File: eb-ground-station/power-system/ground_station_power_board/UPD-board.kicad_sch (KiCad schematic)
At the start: 101 parts, among them J1 Conn_01x04, J10 PI 1827486, J11 PC 1720806, J12 Conn_02x02_Odd_Even, J13 Conn_01x05, J14 Conn_01x04, J2 Conn_01x03, J3 Conn_01x03, J4 Conn_01x03, J5 Conn_01x03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

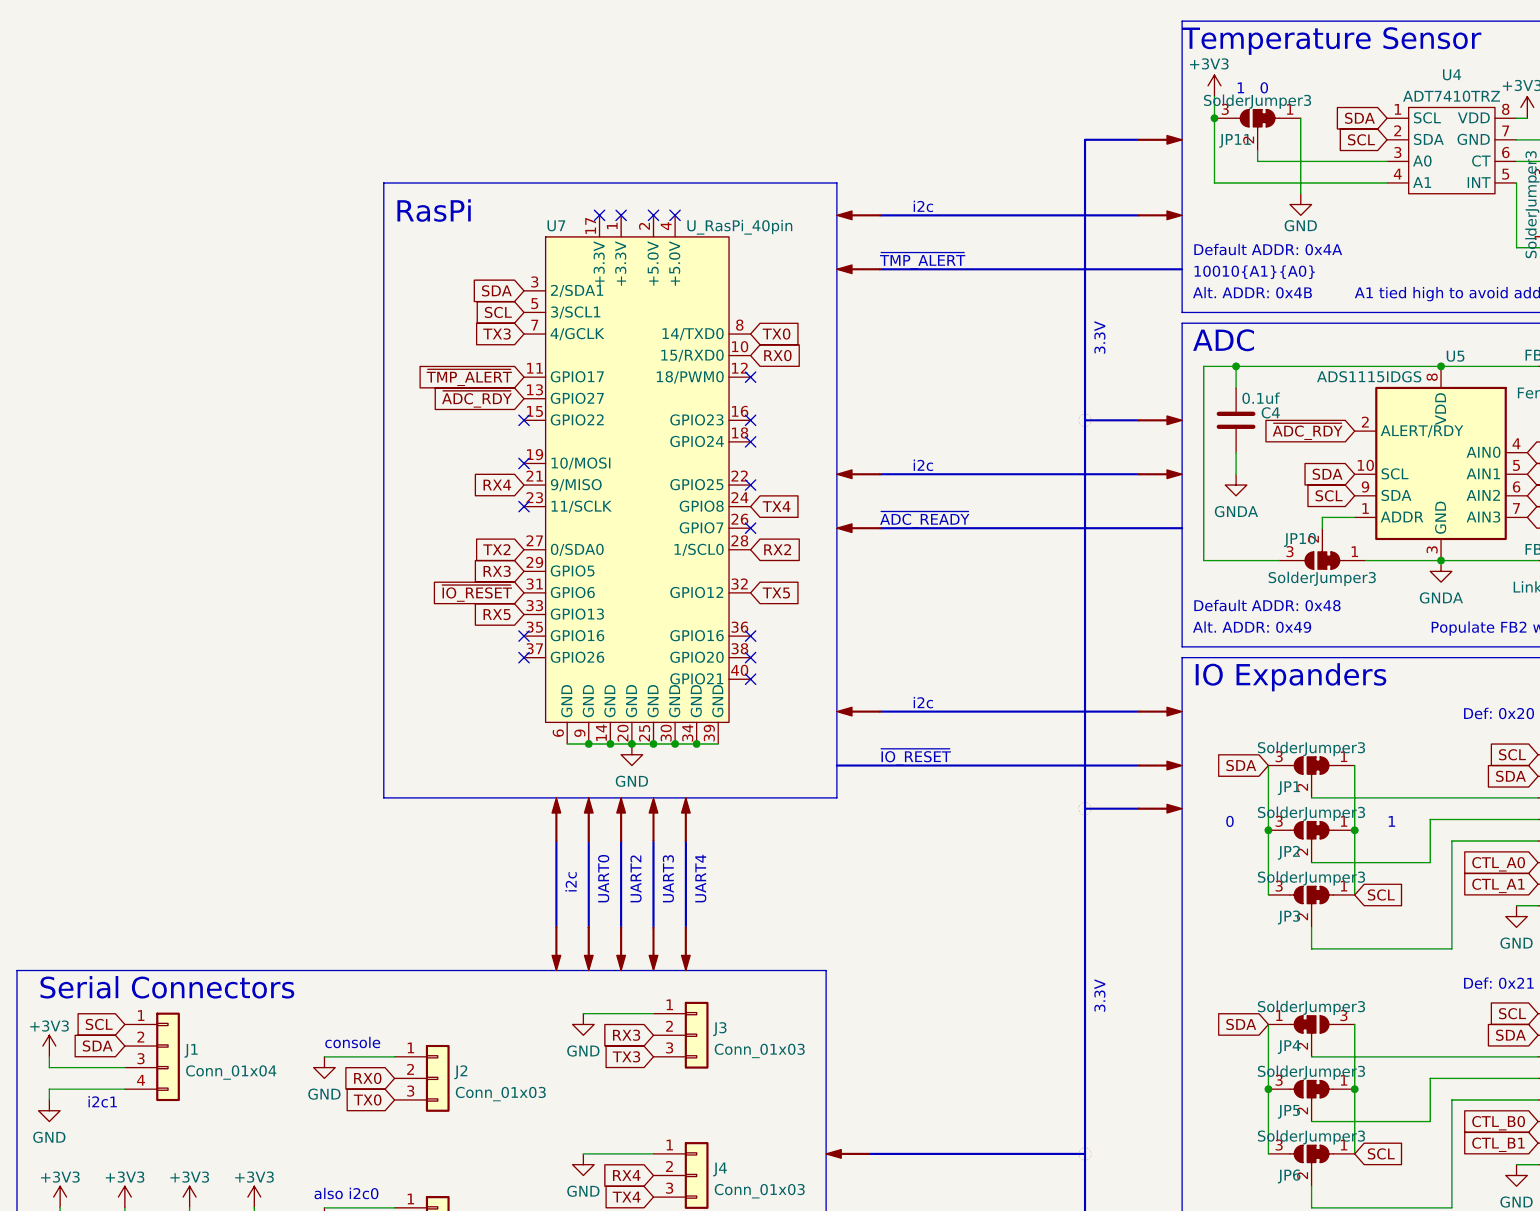
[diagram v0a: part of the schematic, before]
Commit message: Fixed UPD board, ready for review and ordering
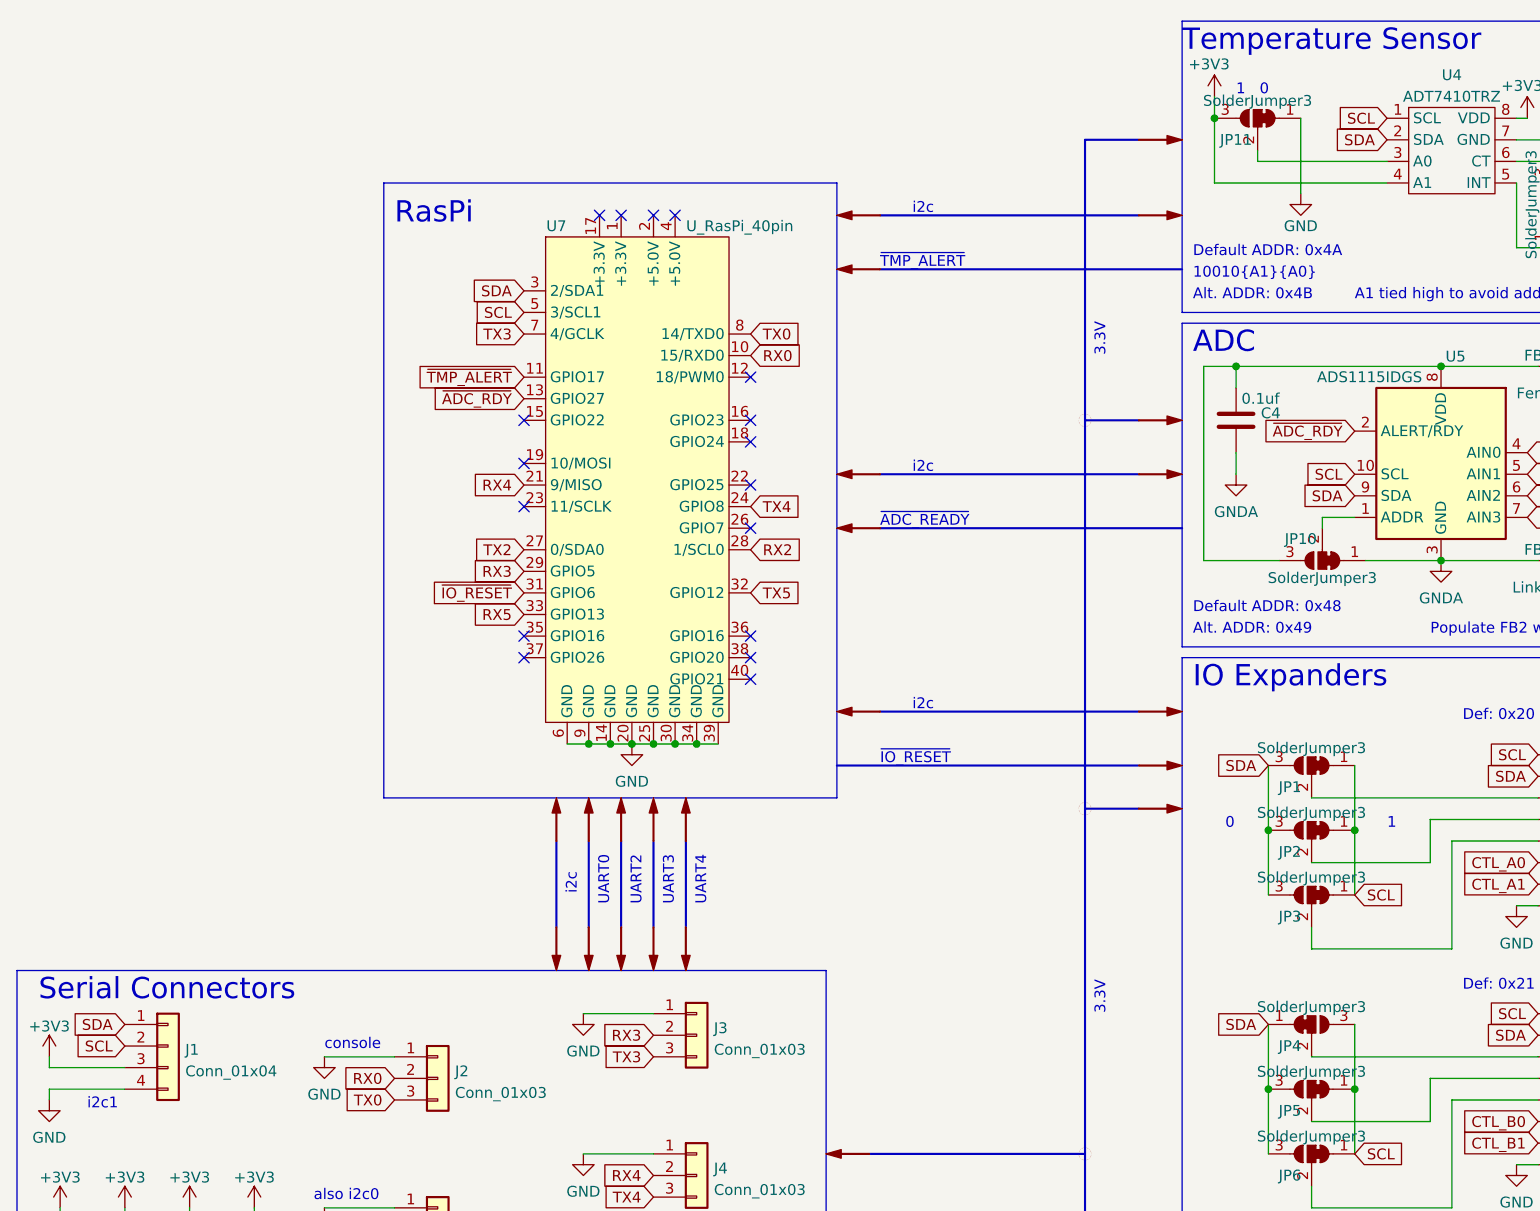
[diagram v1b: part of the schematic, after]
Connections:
- net SCL: now also J1.2 (Pin_2), U4.1 (SCL), U5.10 (SCL); no longer J1.1 (Pin_1), U4.2 (SDA), U5.9 (SDA)
- net SDA: now also J1.1 (Pin_1), U4.2 (SDA), U5.9 (SDA); no longer J1.2 (Pin_2), U4.1 (SCL), U5.10 (SCL)
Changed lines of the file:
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@@
     )
   )
-  (global_label "SDA" (shape input) (at 184.15 68.58 180) (fields_autoplaced)
+  (global_label "SDA" (shape input) (at 184.15 71.12 180) (fields_autoplaced)
     (effects (font (size 1.27 1.27)) (justify right))
-    (property "Intersheet References" "${INTERSHEET_REFS}" (id 0) (at 178.1688 68.5006 0)
+    (property "Intersheet References" "${INTERSHEET_REFS}" (id 0) (at 178.1688 71.0406 0)
       (effects (font (size 1.27 1.27)) (justify right) hide)
     )
@@
     )
   )
-  (global_label "SDA" (shape input) (at 187.96 26.67 180) (fields_autoplaced)
+  (global_label "SDA" (shape input) (at 187.96 29.21 180) (fields_autoplaced)
     (effects (font (size 1.27 1.27)) (justify right))
-    (property "Intersheet References" "${INTERSHEET_REFS}" (id 0) (at 181.9788 26.5906 0)
+    (property "Intersheet References" "${INTERSHEET_REFS}" (id 0) (at 181.9788 29.1306 0)
       (effects (font (size 1.27 1.27)) (justify right) hide)
     )
@@
     )
   )
-  (global_label "SDA" (shape input) (at 39.37 135.89 180) (fields_autoplaced)
+  (global_label "SDA" (shape input) (at 39.37 133.35 180) (fields_autoplaced)
     (effects (font (size 1.27 1.27)) (justify right))
-    (property "Intersheet References" "${INTERSHEET_REFS}" (id 0) (at 33.3888 135.8106 0)
+    (property "Intersheet References" "${INTERSHEET_REFS}" (id 0) (at 33.3888 133.2706 0)
       (effects (font (size 1.27 1.27)) (justify right) hide)
     )
@@
     )
   )
-  (global_label "SCL" (shape input) (at 39.37 133.35 180) (fields_autoplaced)
+  (global_label "SCL" (shape input) (at 39.37 135.89 180) (fields_autoplaced)
     (effects (font (size 1.27 1.27)) (justify right))
-    (property "Intersheet References" "${INTERSHEET_REFS}" (id 0) (at 33.4493 133.2706 0)
+    (property "Intersheet References" "${INTERSHEET_REFS}" (id 0) (at 33.4493 135.8106 0)
       (effects (font (size 1.27 1.27)) (justify right) hide)
     )
@@
     )
   )
-  (global_label "SCL" (shape input) (at 187.96 29.21 180) (fields_autoplaced)
+  (global_label "SCL" (shape input) (at 187.96 26.67 180) (fields_autoplaced)
     (effects (font (size 1.27 1.27)) (justify right))
-    (property "Intersheet References" "${INTERSHEET_REFS}" (id 0) (at 182.0393 29.1306 0)
+    (property "Intersheet References" "${INTERSHEET_REFS}" (id 0) (at 182.0393 26.5906 0)
       (effects (font (size 1.27 1.27)) (justify right) hide)
     )
@@
     )
   )
-  (global_label "SCL" (shape input) (at 184.15 71.12 180) (fields_autoplaced)
+  (global_label "SCL" (shape input) (at 184.15 68.58 180) (fields_autoplaced)
     (effects (font (size 1.27 1.27)) (justify right))
-    (property "Intersheet References" "${INTERSHEET_REFS}" (id 0) (at 178.2293 71.0406 0)
+    (property "Intersheet References" "${INTERSHEET_REFS}" (id 0) (at 178.2293 68.5006 0)
       (effects (font (size 1.27 1.27)) (justify right) hide)
     )
@@
       (reference "LOGO1") (unit 1) (value "OreSat Logo") (footprint "oresat-footprints:logo-small")
     )
-    (path "/3a1c5476-bb6a-4918-80d3-82e1846e9dbb/6f338c88-571d-40d4-a656-bab0f745db42"
+    (path "/3a1c5476-bb6a-4918-80d3-82e1846e9dbb/9b268302-c8f9-4880-a801-2f518477b68a"
       (reference "Q1") (unit 1) (value "DMN61D8L-LVT") (footprint "oresat-footprints:TSOT26-6")
     )
-    (path "/3a1c5476-bb6a-4918-80d3-82e1846e9dbb/9b268302-c8f9-4880-a801-2f518477b68a"
+    (path "/3a1c5476-bb6a-4918-80d3-82e1846e9dbb/6f338c88-571d-40d4-a656-bab0f745db42"
       (reference "Q1") (unit 2) (value "DMN61D8L-LVT") (footprint "oresat-footprints:TSOT26-6")
     )
@@
       (reference "Q3") (unit 1) (value "SUD50P08-25L-E3") (footprint "oresat-footprints:TO-252-3_TabIsPin2")
     )
-    (path "/3a1c5476-bb6a-4918-80d3-82e1846e9dbb/94011d84-c031-4181-9a68-89df89d536a3"
+    (path "/3a1c5476-bb6a-4918-80d3-82e1846e9dbb/deaca104-2c5f-455a-9001-3371e3306116"
       (reference "Q4") (unit 1) (value "DMN61D8L-LVT") (footprint "oresat-footprints:TSOT26-6")
     )
-    (path "/3a1c5476-bb6a-4918-80d3-82e1846e9dbb/deaca104-2c5f-455a-9001-3371e3306116"
+    (path "/3a1c5476-bb6a-4918-80d3-82e1846e9dbb/94011d84-c031-4181-9a68-89df89d536a3"
       (reference "Q4") (unit 2) (value "DMN61D8L-LVT") (footprint "oresat-footprints:TSOT26-6")
     )
@@
       (reference "Q6") (unit 1) (value "SUD50P08-25L-E3") (footprint "oresat-footprints:TO-252-3_TabIsPin2")
     )
-    (path "/3a1c5476-bb6a-4918-80d3-82e1846e9dbb/11b9c0f2-a612-4d52-85f4-d7fb97bd55bd"
+    (path "/3a1c5476-bb6a-4918-80d3-82e1846e9dbb/12ff1775-db0b-4f93-8454-17de940e4617"
       (reference "Q7") (unit 1) (value "DMN61D8L-LVT") (footprint "oresat-footprints:TSOT26-6")
     )
-    (path "/3a1c5476-bb6a-4918-80d3-82e1846e9dbb/12ff1775-db0b-4f93-8454-17de940e4617"
+    (path "/3a1c5476-bb6a-4918-80d3-82e1846e9dbb/11b9c0f2-a612-4d52-85f4-d7fb97bd55bd"
       (reference "Q7") (unit 2) (value "DMN61D8L-LVT") (footprint "oresat-footprints:TSOT26-6")
     )
@@
       (reference "Q9") (unit 1) (value "SUD50P08-25L-E3") (footprint "oresat-footprints:TO-252-3_TabIsPin2")
     )
-    (path "/3a1c5476-bb6a-4918-80d3-82e1846e9dbb/777a7611-3f95-4b63-882e-22837a921249"
+    (path "/3a1c5476-bb6a-4918-80d3-82e1846e9dbb/7846e60b-2e16-4833-b5a0-71b3e5a6fdb8"
       (reference "Q10") (unit 1) (value "DMN61D8L-LVT") (footprint "oresat-footprints:TSOT26-6")
     )
-    (path "/3a1c5476-bb6a-4918-80d3-82e1846e9dbb/7846e60b-2e16-4833-b5a0-71b3e5a6fdb8"
+    (path "/3a1c5476-bb6a-4918-80d3-82e1846e9dbb/777a7611-3f95-4b63-882e-22837a921249"
       (reference "Q10") (unit 2) (value "DMN61D8L-LVT") (footprint "oresat-footprints:TSOT26-6")
     )

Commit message: Fixed pin 1 of expanders being pulldown only
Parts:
- LOGO1: footprint oresat-footprints:logo-small -> oresat-graphics:logo-small
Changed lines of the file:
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@@
     )
     (property "Value" "OreSat Logo" (id 1) (at 410.21 259.08 0))
-    (property "Footprint" "oresat-footprints:logo-small" (id 2) (at 402.59 259.08 0)
+    (property "Footprint" "oresat-graphics:logo-small" (id 2) (at 402.59 259.08 0)
       (effects (font (size 1.27 1.27)) hide)
     )
@@
       (reference "#PWR0109") (unit 1) (value "GND") (footprint "")
     )
+    (path "/3a1c5476-bb6a-4918-80d3-82e1846e9dbb/8455e93e-0497-4a1b-98ad-a5ed8aa30439"
+      (reference "#PWR0110") (unit 1) (value "+3V3") (footprint "")
+    )
     (path "/3a1c5476-bb6a-4918-80d3-82e1846e9dbb/84c28457-6e31-4c65-8539-377808b3bd60"
       (reference "#PWR0111") (unit 1) (value "GND") (footprint "")
@@
     )
     (path "/fd8cf496-8078-42c7-846c-0a70693744f4"
-      (reference "LOGO1") (unit 1) (value "OreSat Logo") (footprint "oresat-footprints:logo-small")
+      (reference "LOGO1") (unit 1) (value "OreSat Logo") (footprint "oresat-graphics:logo-small")
     )
     (path "/3a1c5476-bb6a-4918-80d3-82e1846e9dbb/9b268302-c8f9-4880-a801-2f518477b68a"
